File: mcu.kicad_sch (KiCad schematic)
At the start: 61 parts, among them J10 PinHeader_2x10_P1.27mm_SMD_Sh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, SW5 SW_B3U-1000P_SMD, SW6 CAS-120TA, U1 STM32H753ZIT6, Y1 Resonator_32.768kHz_ECX-31B, Y2 Oscillator_25MHz_ESC_2016MV

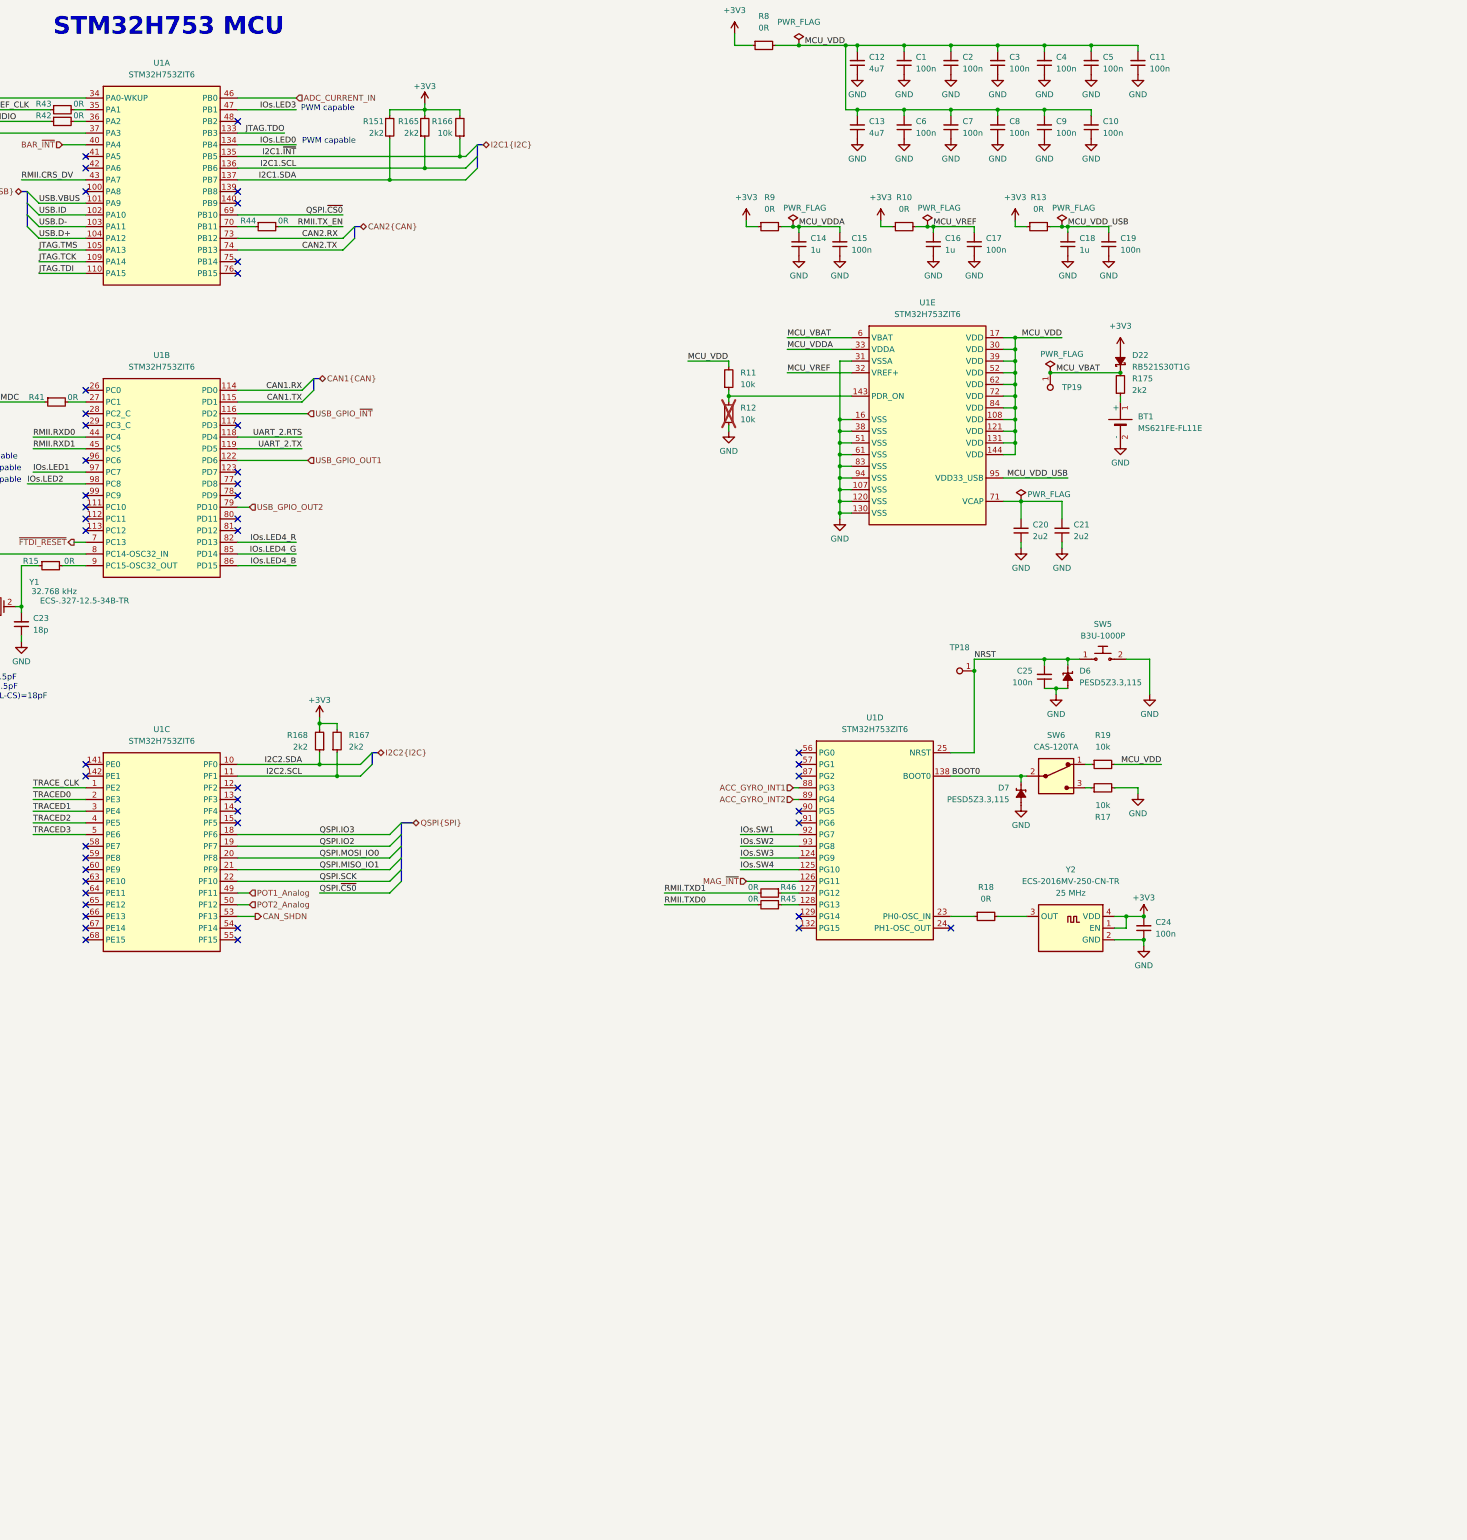
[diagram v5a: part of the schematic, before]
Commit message: [#95398] Mock main components, add BGA MCU
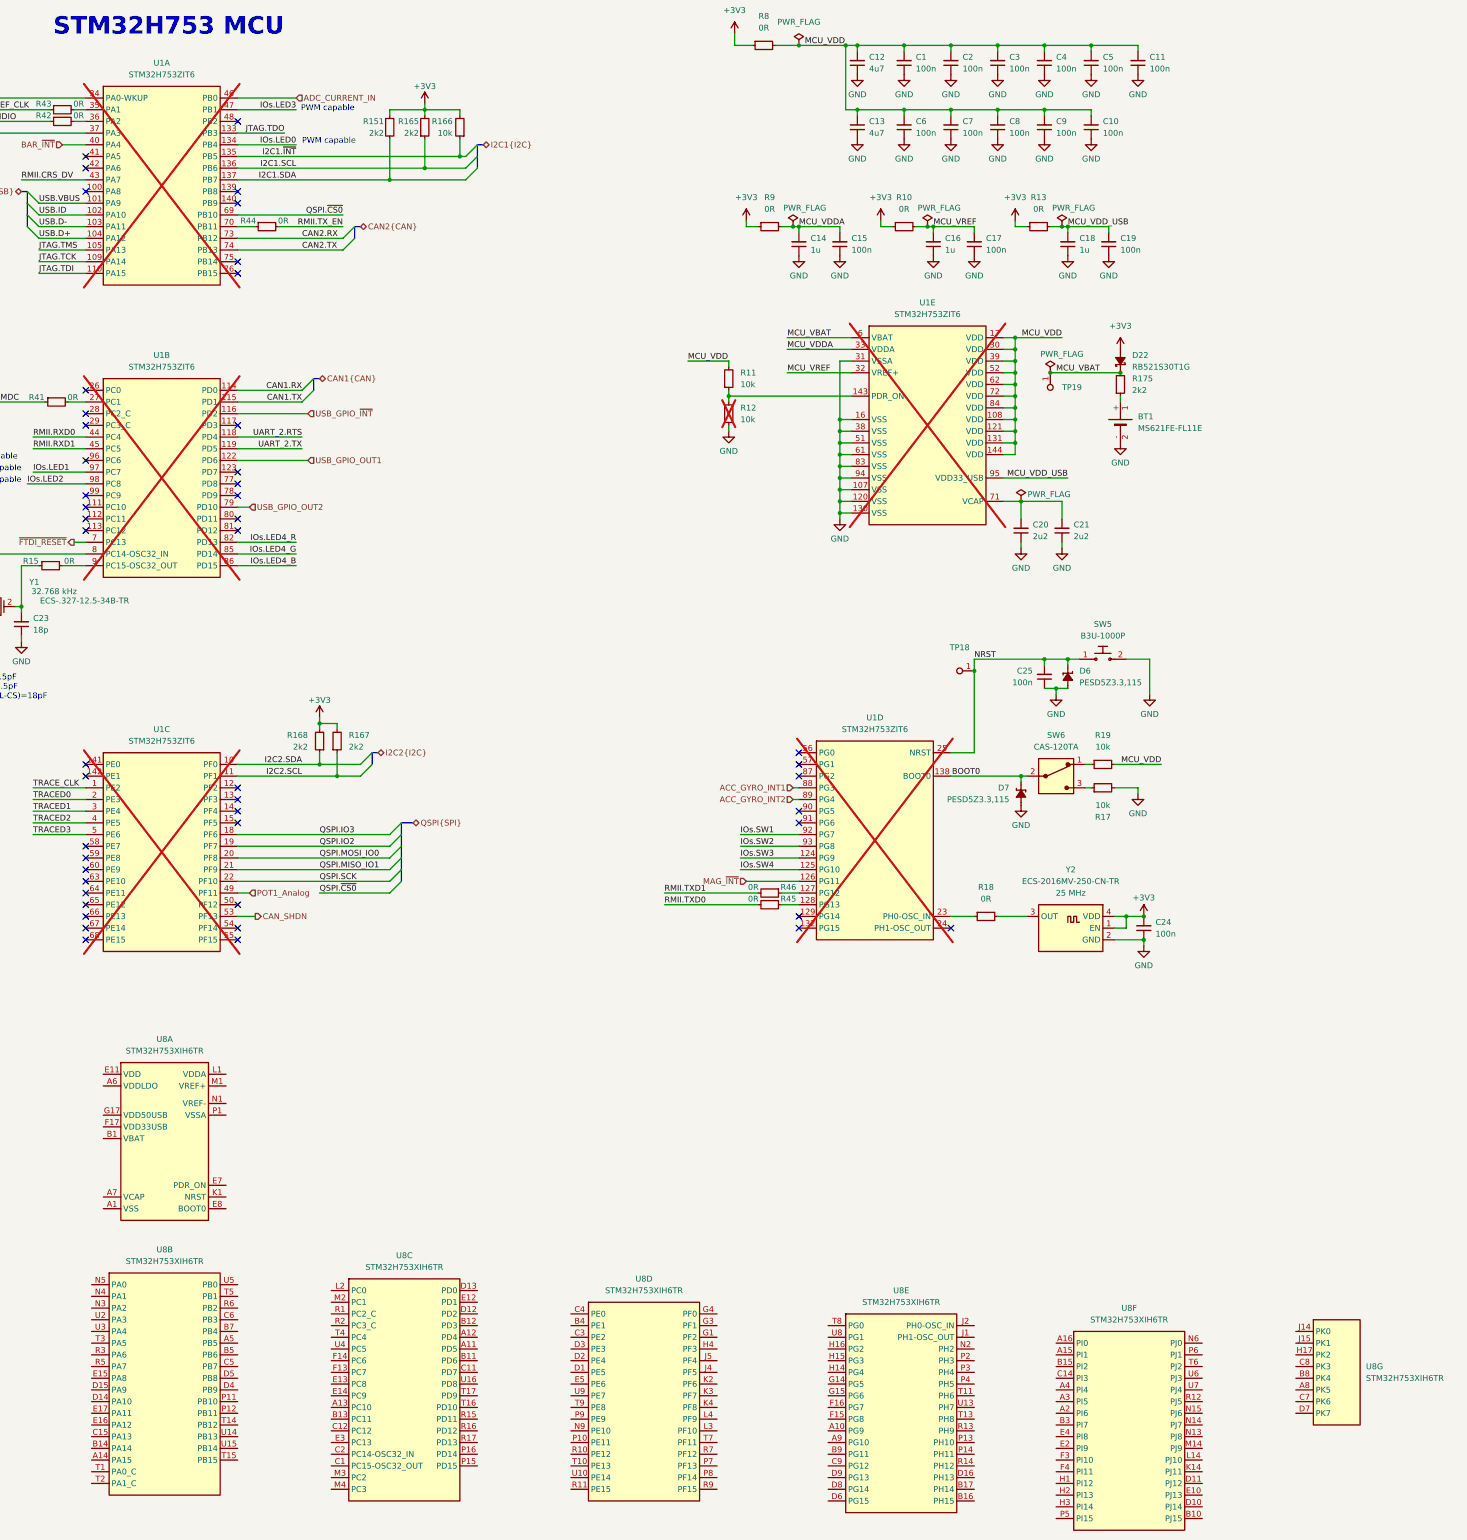
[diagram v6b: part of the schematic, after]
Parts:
- added U8: STM32H753XIH6, antmicro-footprints:TFBGA-289-265_14x14mm_Layout17x17_P0.8mm, symbol antmicroMicrocontrollers:STM32H753XIH6
- U1: now not fitted
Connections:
- net POT2_Analog: no longer names the net of U1.50 (PF12)
- new net: U8.A1 (VSS), U8.A17 (VSS), U8.B2 (VSS), U8.B6 (VSS), U8.C10 (VSS), U8.C13 (VSS), U8.C16 (VSS), U8.F1 (VSS), U8.F2 (VSS), U8.G10 (VSS), U8.G11 (VSS), U8.G16 (VSS), U8.G2 (VSS), U8.G7 (VSS), U8.G8 (VSS), U8.G9 (VSS), U8.H10 (VSS), U8.H11 (VSS), U8.H7 (VSS), U8.H8 (VSS), U8.H9 (VSS), U8.J10 (VSS), U8.J11 (VSS), U8.J16 (VSS), U8.J17 (VSS), U8.J3 (VSS), U8.J7 (VSS), U8.J8 (VSS), U8.J9 (VSS), U8.K10 (VSS), U8.K11 (VSS), U8.K15 (VSS), U8.K7 (VSS), U8.K8 (VSS), U8.K9 (VSS), U8.L10 (VSS), U8.L11 (VSS), U8.L15 (VSS), U8.L7 (VSS), U8.L8 (VSS), U8.L9 (VSS), U8.M15 (VSS), U8.N16 (VSS), U8.R4 (VSS), U8.R8 (VSS), U8.T12 (VSS), U8.U1 (VSS), U8.U17 (VSS)
- new net: U8.A6 (VDDLDO), U8.C17 (VDDLDO), U8.U12 (VDDLDO)
- new net: U8.A7 (VCAP), U8.D17 (VCAP), U8.U11 (VCAP)
- new net: U8.E1 (NC), U8.K16 (NC), U8.K17 (NC), U8.L16 (NC), U8.L17 (NC), U8.M16 (NC), U8.M17 (NC), U8.N17 (NC)
- new net: U8.E11 (VDD), U8.E6 (VDD), U8.E9 (VDD), U8.F5 (VDD), U8.G13 (VDD), U8.G5 (VDD), U8.H13 (VDD), U8.H5 (VDD), U8.J13 (VDD), U8.K13 (VDD), U8.K5 (VDD), U8.L13 (VDD), U8.L5 (VDD), U8.M13 (VDD), U8.M5 (VDD), U8.N10 (VDD), U8.N11 (VDD), U8.N12 (VDD), U8.N7 (VDD), U8.N8 (VDD), U8.P17 (VDD)
- no-connect marks 48 -> 49

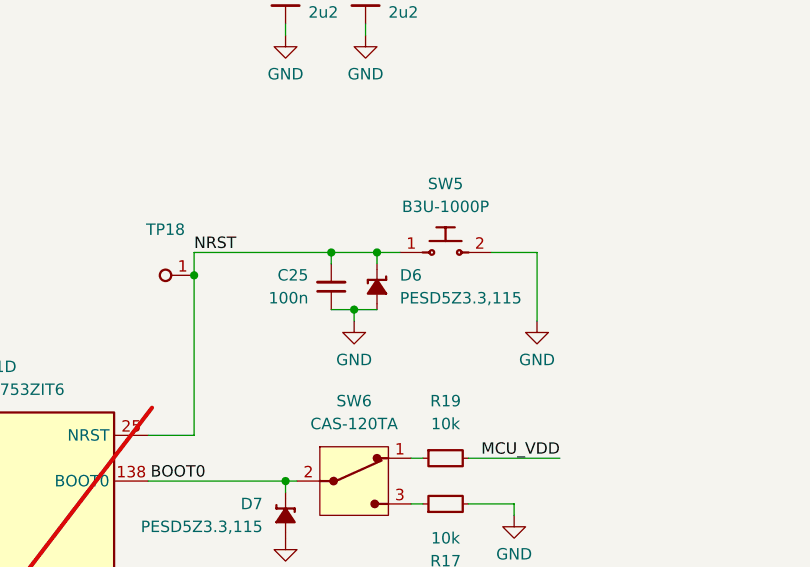
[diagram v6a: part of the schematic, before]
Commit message: [#95398] Replace reset button
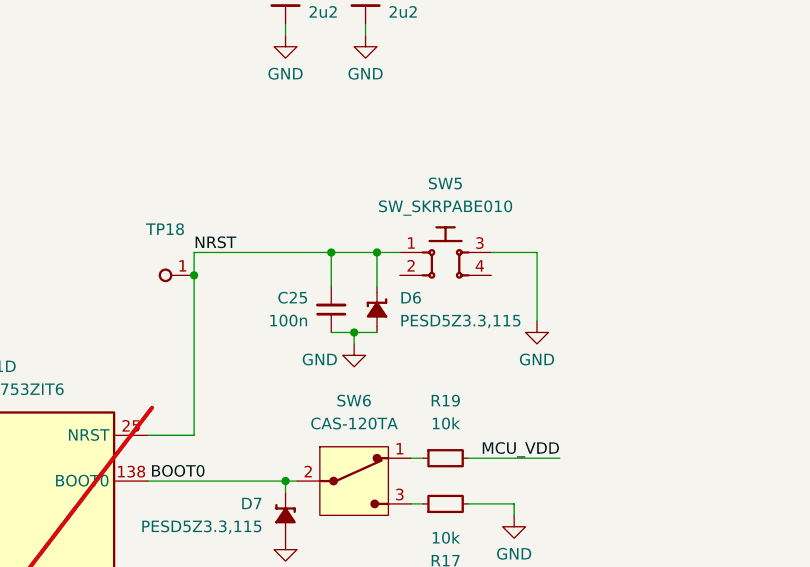
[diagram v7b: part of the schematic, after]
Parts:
- removed SW5: SW_B3U-1000P_SMD, antmicro-footprints:SW_B3U-1000P_SMD, symbol antmicroPushbuttonSwitches:SW_B3U-1000P_SMD
- added SW5: SW_SKRPABE010, antmicro-footprints:SW_PTS810SJM250SMTRLFS_SMD, symbol antmicroPushbuttonSwitches:SW_SKRPABE010
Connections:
- net GND: now also SW5.3
- net NRST: now also SW5.1
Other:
- moved on the sheet: C25, D6
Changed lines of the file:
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@@
 	)
 	(junction
-		(at 373.38 167.64)
+		(at 373.38 170.18)
 		(diameter 0)
 		(color 0 0 0 0)
@@
 	(wire
 		(pts
-			(xy 373.38 167.64) (xy 373.38 168.91)
+			(xy 373.38 170.18) (xy 373.38 171.45)
 		)
 		(stroke
@@
 	(wire
 		(pts
-			(xy 370.84 167.64) (xy 373.38 167.64)
+			(xy 370.84 170.18) (xy 373.38 170.18)
 		)
 		(stroke
@@
 	(wire
 		(pts
-			(xy 375.92 162.56) (xy 375.92 161.29)
+			(xy 375.92 165.1) (xy 375.92 161.29)
 		)
 		(stroke
@@
 	(wire
 		(pts
-			(xy 373.38 167.64) (xy 375.92 167.64)
+			(xy 373.38 170.18) (xy 375.92 170.18)
 		)
 		(stroke
@@
 	(wire
 		(pts
-			(xy 370.84 161.29) (xy 370.84 162.56)
+			(xy 370.84 161.29) (xy 370.84 165.1)
 		)
 		(stroke
@@
 	(symbol
 		(lib_id "antmicroCapacitors0402:C_100n_0402")
-		(at 370.84 167.64 270)
+		(at 370.84 170.18 270)
 		(mirror x)
 		(unit 1)
@@
 		(dnp no)
 		(property "Reference" "C25"
-			(at 368.3 163.8236 90)
+			(at 368.3 166.3636 90)
 			(effects
 				(font
@@
 		)
 		(property "Value" "C_100n_0402"
-			(at 360.68 147.32 0)
+			(at 360.68 149.86 0)
 			(effects
 				(font
@@
 		)
 		(property "Footprint" "antmicro-footprints:C_0402_1005Metric"
-			(at 358.14 147.32 0)
+			(at 358.14 149.86 0)
 			(effects
 				(font
@@
 		)
 		(property "Datasheet" "https://www.murata.com/products/productdetail?partno=GRM155R61H104KE14%23"
-			(at 355.6 147.32 0)
+			(at 355.6 149.86 0)
 			(effects
 				(font
@@
 		)
 		(property "Description" "SMD Multilayer Ceramic Capacitor, 0.1 µF, 50 V, 0402 [1005 Metric], ± 10%, X5R, GRM Series"
-			(at 337.82 147.32 0)
+			(at 337.82 149.86 0)
 			(effects
 				(font
@@
 		)
 		(property "MPN" "GRM155R61H104KE14D"
-			(at 353.06 147.32 0)
+			(at 353.06 149.86 0)
 			(effects
 				(font
@@
 		)
 		(property "Manufacturer" "Murata"
-			(at 350.52 147.32 0)
+			(at 350.52 149.86 0)
 			(effects
 				(font
@@
 		)
 		(property "License" "Apache-2.0"
-			(at 347.98 147.32 0)
+			(at 347.98 149.86 0)
 			(effects
 				(font
@@
 		)
 		(property "Author" "Antmicro"
-			(at 345.44 147.32 0)
+			(at 345.44 149.86 0)
 			(effects
 				(font
@@
 		)
 		(property "Val" "100n"
-			(at 368.3 166.3636 90)
+			(at 368.3 168.9036 90)
 			(effects
 				(font
@@
 		)
 		(property "Voltage" "50V"
-			(at 342.9 147.32 0)
+			(at 342.9 149.86 0)
 			(effects
 				(font
@@
 		)
 		(property "Dielectric" "X5R"
-			(at 340.36 147.32 0)
+			(at 340.36 149.86 0)
 			(effects
 				(font
@@
 	)
 	(symbol
-		(lib_id "antmicroPushbuttonSwitches:SW_B3U-1000P_SMD")
+		(lib_id "antmicroPushbuttonSwitches:SW_SKRPABE010")
 		(at 378.46 161.29 0)
 		(unit 1)
@@
 			)
 		)
-		(property "Value" "SW_B3U-1000P_SMD"
-			(at 403.86 166.37 0)
+		(property "Value" "SW_SKRPABE010"
+			(at 383.54 156.21 0)
 			(effects
 				(font
@@
 					(thickness 0.15)
 				)
-				(justify left bottom)
-				(hide yes)
 			)
 		)
-		(property "Footprint" "antmicro-footprints:SW_B3U-1000P_SMD"
-			(at 403.86 168.91 0)
+		(property "Footprint" "antmicro-footprints:SW_PTS810SJM250SMTRLFS_SMD"
+			(at 400.05 168.91 0)
 			(effects
 				(font
@@
 			)
 		)
-		(property "Datasheet" "https://omronfs.omron.com/en_US/ecb/products/pdf/en-b3u.pdf"
-			(at 403.86 171.45 0)
+		(property "Datasheet" "https://tech.alpsalpine.com/e/products/detail/SKRPABE010/"
+			(at 400.05 171.45 0)
 			(effects
 				(font
@@
 			)
 		)
-		(property "Description" "Tactile Switch, B3U, Top Actuated, Surface Mount, Round Button, 153 gf, 50mA at 12VDC"
-			(at 403.86 184.15 0)
+		(property "Description" "Tactile Switch, PTS810, Top Actuated, Surface Mount, Oval Button, 160 gf, 50mA at 16VDC"
+			(at 400.05 184.15 0)
 			(effects
 				(font
@@
 			)
 		)
-		(property "MPN" "B3U-1000P"
-			(at 383.54 156.21 0)
+		(property "MPN" "SKRPABE010"
+			(at 400.05 173.99 0)
 			(effects
 				(font
@@
 					(thickness 0.15)
 				)
+				(justify left bottom)
+				(hide yes)
 			)
 		)
-		(property "Manufacturer" "Omron"
-			(at 403.86 176.53 0)
+		(property "Manufacturer" "Alps Alpine"
+			(at 400.05 176.53 0)
 			(effects
 				(font
@@
 		)
 		(property "Author" "Antmicro"
-			(at 403.86 179.07 0)
+			(at 400.05 179.07 0)
 			(effects
 				(font
@@
 		)
 		(property "License" "Apache-2.0"
-			(at 403.86 181.61 0)
+			(at 400.05 181.61 0)
 			(effects
 				(font
@@
 			)
 		)
+		(pin "4"
+		)
+		(pin "3"
+		)
 		(pin "1"
 		)
@@
 	(symbol
 		(lib_id "antmicroTVSDiodes:PESD5Z3.3")
-		(at 375.92 162.56 270)
+		(at 375.92 165.1 270)
 		(unit 1)
 		(exclude_from_sim no)
@@
 		(fields_autoplaced yes)
 		(property "Reference" "D6"
-			(at 378.46 163.83 90)
+			(at 378.46 166.37 90)
 			(effects
 				(font
@@
 		)
 		(property "Value" "PESD5Z3.3"
-			(at 363.22 177.8 0)
+			(at 363.22 180.34 0)
 			(effects
 				(font
@@
 		)
 		(property "Footprint" "antmicro-footprints:SOD-523"
-			(at 370.84 177.8 0)
+			(at 370.84 180.34 0)
 			(effects
 				(font
@@
 		)
 		(property "Datasheet" "https://assets.nexperia.com/documents/data-sheet/PESD5Z3_3.pdf"
-			(at 368.3 177.8 0)
+			(at 368.3 180.34 0)
 			(effects
 				(font
@@
 		)
 		(property "Description" "Unidirectional TVS, 30 kV,  SOD-523, 3.3 V, 172 pF"
-			(at 355.6 177.8 0)
+			(at 355.6 180.34 0)
 			(effects
 				(font
@@
 		)
 		(property "Manufacturer" "Nexperia"
-			(at 365.76 177.8 0)
+			(at 365.76 180.34 0)
 			(effects
 				(font
@@
 		)
 		(property "MPN" "PESD5Z3.3,115"
-			(at 378.46 166.37 90)
+			(at 378.46 168.91 90)
 			(effects
 				(font
@@
 		)
 		(property "Author" "Antmicro"
-			(at 360.68 177.8 0)
+			(at 360.68 180.34 0)
 			(effects
 				(font
@@
 		)
 		(property "License" "Apache-2.0"
-			(at 358.14 177.8 0)
+			(at 358.14 180.34 0)
 			(effects
 				(font
@@
 	(symbol
 		(lib_id "antmicropower:GND")
-		(at 373.38 168.91 0)
+		(at 373.38 171.45 0)
 		(unit 1)
 		(exclude_from_sim no)
@@
 		(dnp no)
 		(property "Reference" "#PWR043"
-			(at 382.27 171.45 0)
+			(at 382.27 173.99 0)
 			(effects
 				(font
@@
 		)
 		(property "Value" "GND"
-			(at 373.38 173.228 0)
+			(at 369.57 173.228 0)
 			(effects
 				(font
@@
 		)
 		(property "Footprint" ""
-			(at 382.27 176.53 0)
+			(at 382.27 179.07 0)
 			(effects
 				(font
@@
 		)
 		(property "Datasheet" ""
-			(at 382.27 181.61 0)
+			(at 382.27 184.15 0)
 			(effects
 				(font
@@
 		)
 		(property "Description" ""
-			(at 382.27 184.15 0)
+			(at 382.27 186.69 0)
 			(effects
 				(font
@@
 		)
 		(property "Author" "Antmicro"
-			(at 382.27 176.53 0)
+			(at 382.27 179.07 0)
 			(effects
 				(font
@@
 		)
 		(property "License" "Apache-2.0"
-			(at 382.27 179.07 0)
+			(at 382.27 181.61 0)
 			(effects
 				(font

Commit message: [#95398] Implement basic post review sugestions
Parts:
- removed R10, R13, R8, R9: R_0R_0402, antmicro-footprints:R_0402_1005Metric, symbol antmicroResistors0402:R_0R_0402
- added FB1: FB_1k5Z_0.5A_Murata-BLM18HE_0603, antmicro-footprints:FB_0603_1608Metric, symbol antmicroFerriteBeadsandChips:FB_1k5Z_0.5A_Murata-BLM18HE_0603
- added R102: R_33k_0402, antmicro-footprints:R_0402_1005Metric, symbol antmicroResistors0402:R_33k_0402
- added R103: R_82k_0402, antmicro-footprints:R_0402_1005Metric, symbol antmicroResistors0402:R_82k_0402
- added R140: R_10k_0402, antmicro-footprints:R_0402_1005Metric, symbol antmicroResistors0402:R_10k_0402
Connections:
- net MCU_VDD is gone; now on net +3V3: C1.2, C10.2, C11.2, C12.2, C13.2, C2.2, C3.2, C4.2, C5.2, C6.2, C7.2, C8.2, C9.2, R11.2, R19.2, U1.108 (VDD), U1.121 (VDD), U1.131 (VDD), U1.144 (VDD), U1.17 (VDD), U1.30 (VDD), U1.39 (VDD), U1.52 (VDD), U1.62 (VDD), U1.72 (VDD), U1.84 (VDD)
- net MCU_VDD_USB is gone; now on net +3V3: C18.2, C19.2, U1.95 (VDD33_USB)
- net MCU_VREF is gone; now on net +3V3: C16.2, C17.2, U1.32 (VREF+)
- net +3V3: now also FB1.1, R140.2
- net GND: now also R103.1
- net MCU_VDDA: now also FB1.2
- net NRST: now also R140.1
- net USB.VBUS: now also R102.2; no longer U1.101 (PA9)
- new net USB_VBUS: R102.1, R103.2, U1.101 (PA9)
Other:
- note added: "MCU_VDD"
- note added: "MCU_VDD_USB"
- note added: "MCU_VREF"
